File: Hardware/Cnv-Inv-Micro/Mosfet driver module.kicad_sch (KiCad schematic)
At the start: 14 parts, among them Q7 SS8050, Q8 SS8050, U6 6N135, U7 6N135, U8 IR2104

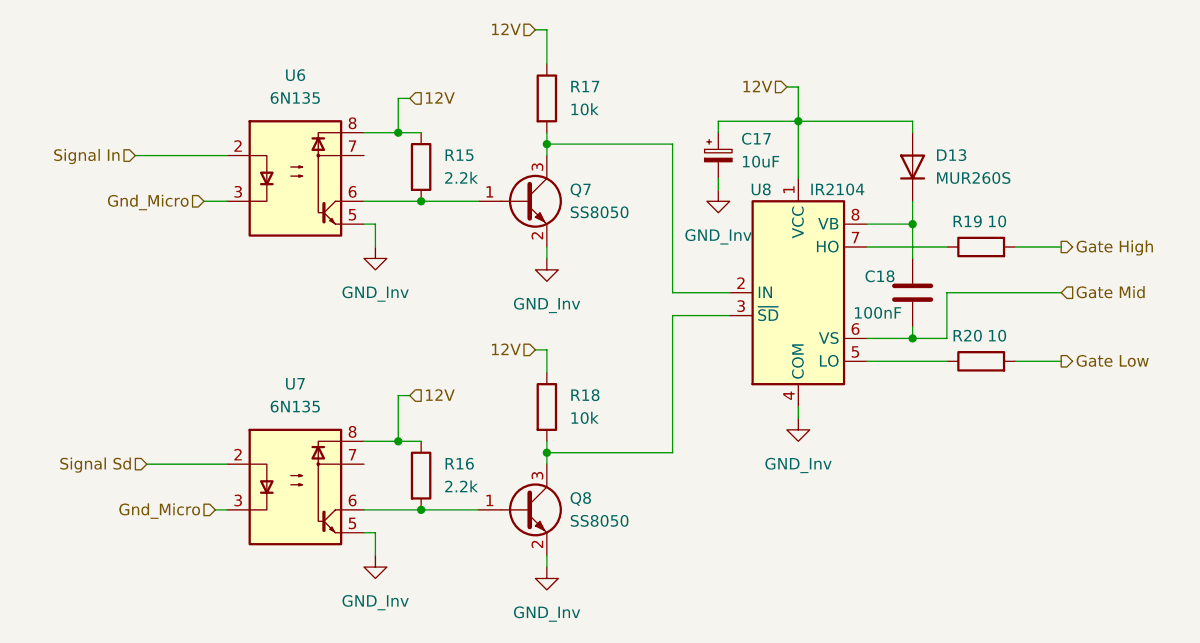
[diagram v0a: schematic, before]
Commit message: Avances en PCB conversor y inversor - Simulaciones de modulacion
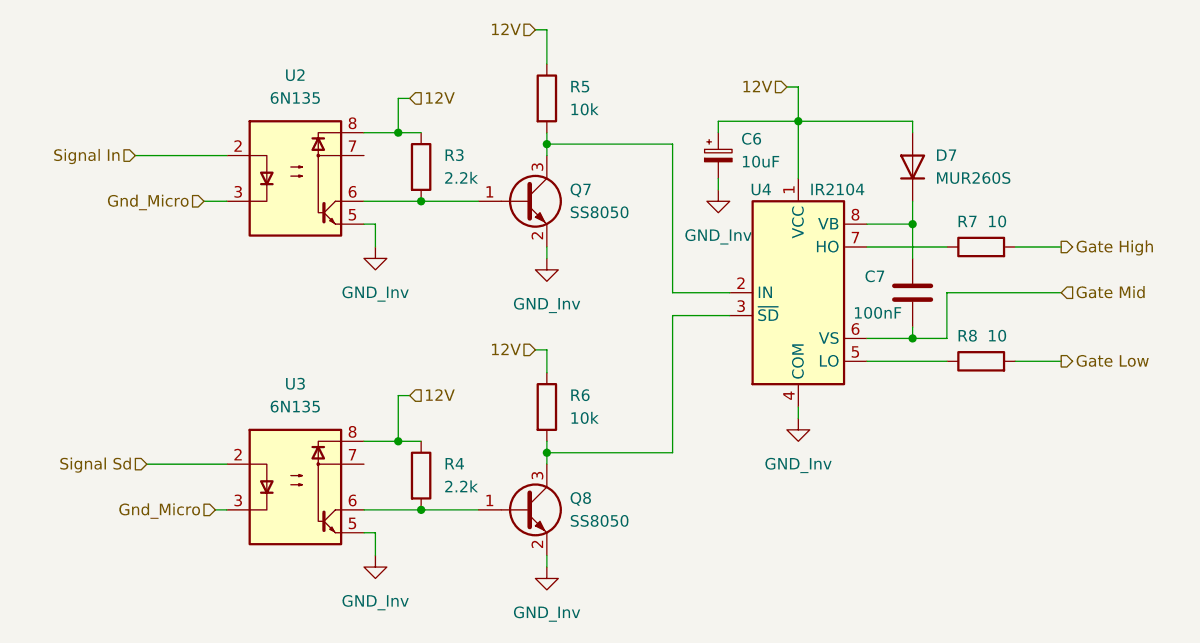
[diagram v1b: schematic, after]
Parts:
- U2: renamed from U6; footprint Package_DIP:DIP-8_W7.62mm -> Package_SO:SOP-8_6.62x9.15mm_P2.54mm
- U3: renamed from U7; footprint Package_DIP:DIP-8_W7.62mm -> Package_SO:SOP-8_6.62x9.15mm_P2.54mm
- renumbered C17 to C6, C18 to C7, D13 to D7, R15 to R3, R16 to R4, R17 to R5, R18 to R6, R19 to R7, R20 to R8, U8 to U4
